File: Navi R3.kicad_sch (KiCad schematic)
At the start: 66 parts, among them J1 USB_C_Receptacle_USB2.0_16P, J2 Conn_01x02_Pin, J3 Conn_01x02_Pin, J4 Conn_01x03_Socket, J5 Conn_02x03_Counter_Clockwise, SW1 SW_Push, SW2 D2FC-F-7N20M, SW3 D2FC-F-7N20M, SW4 D2FC-F-7N20M, SW5 SW_Push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

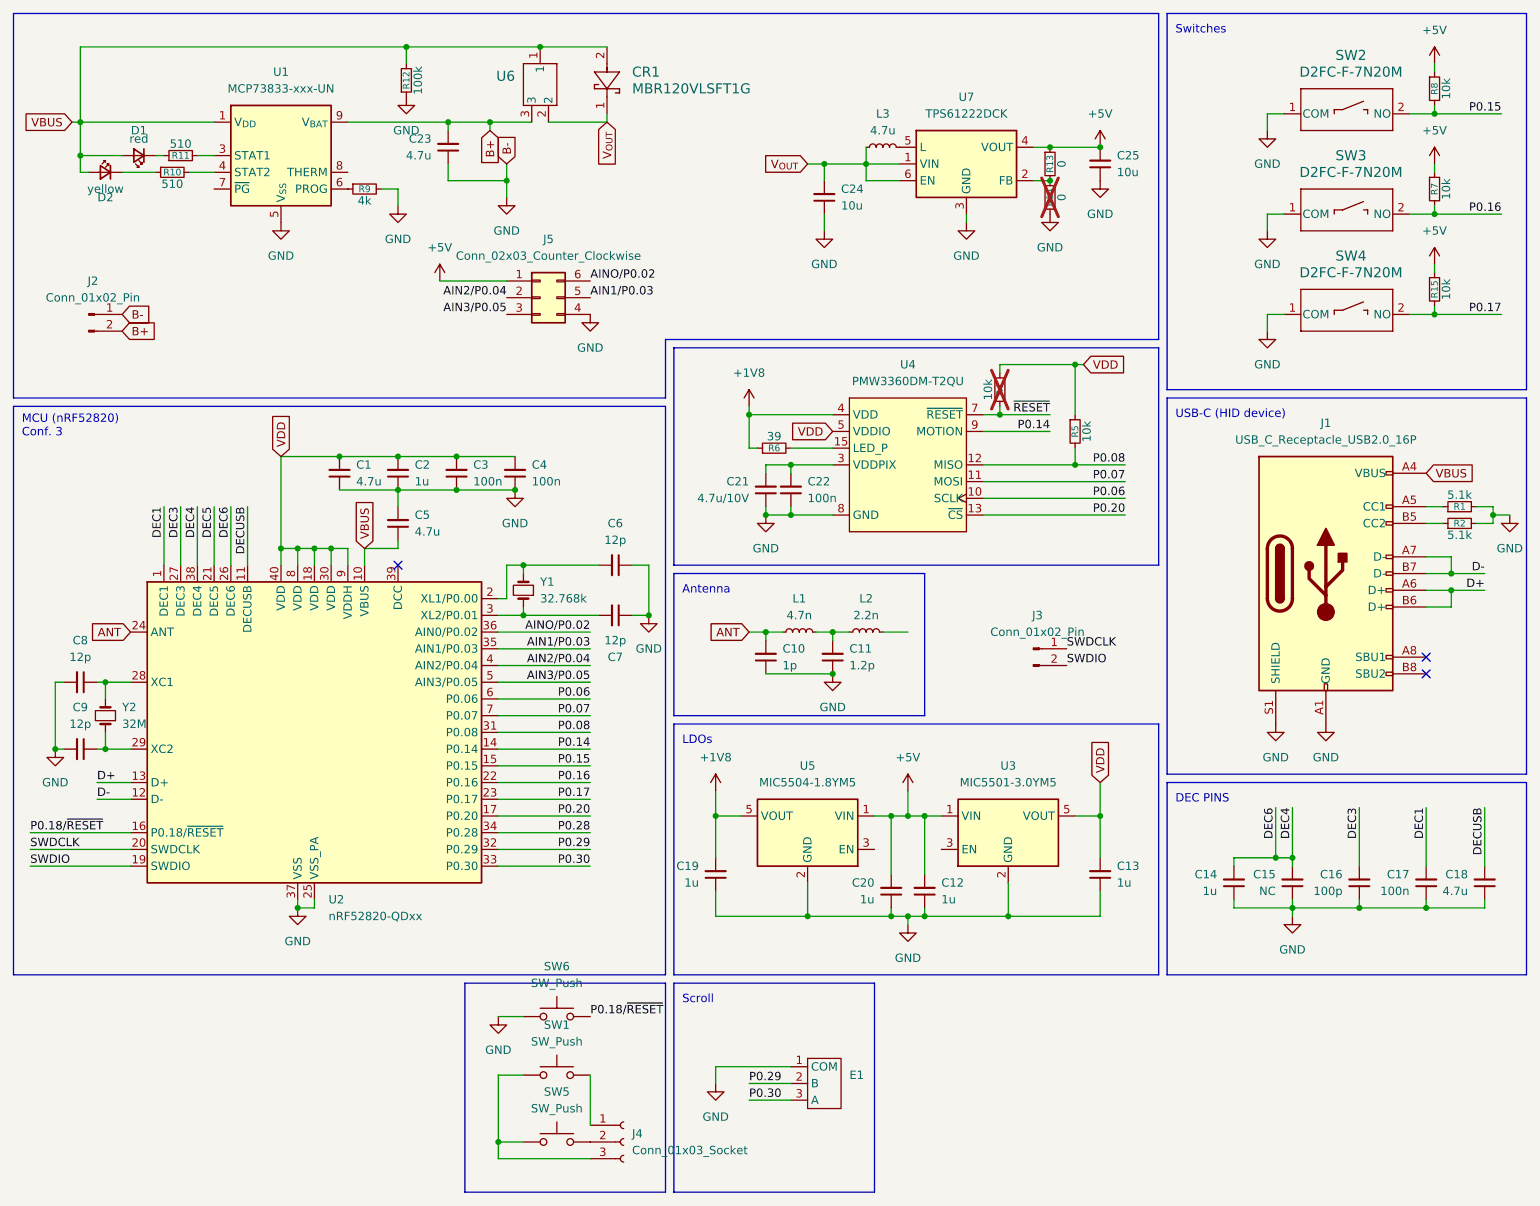
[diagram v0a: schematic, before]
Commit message: Update SWD headers
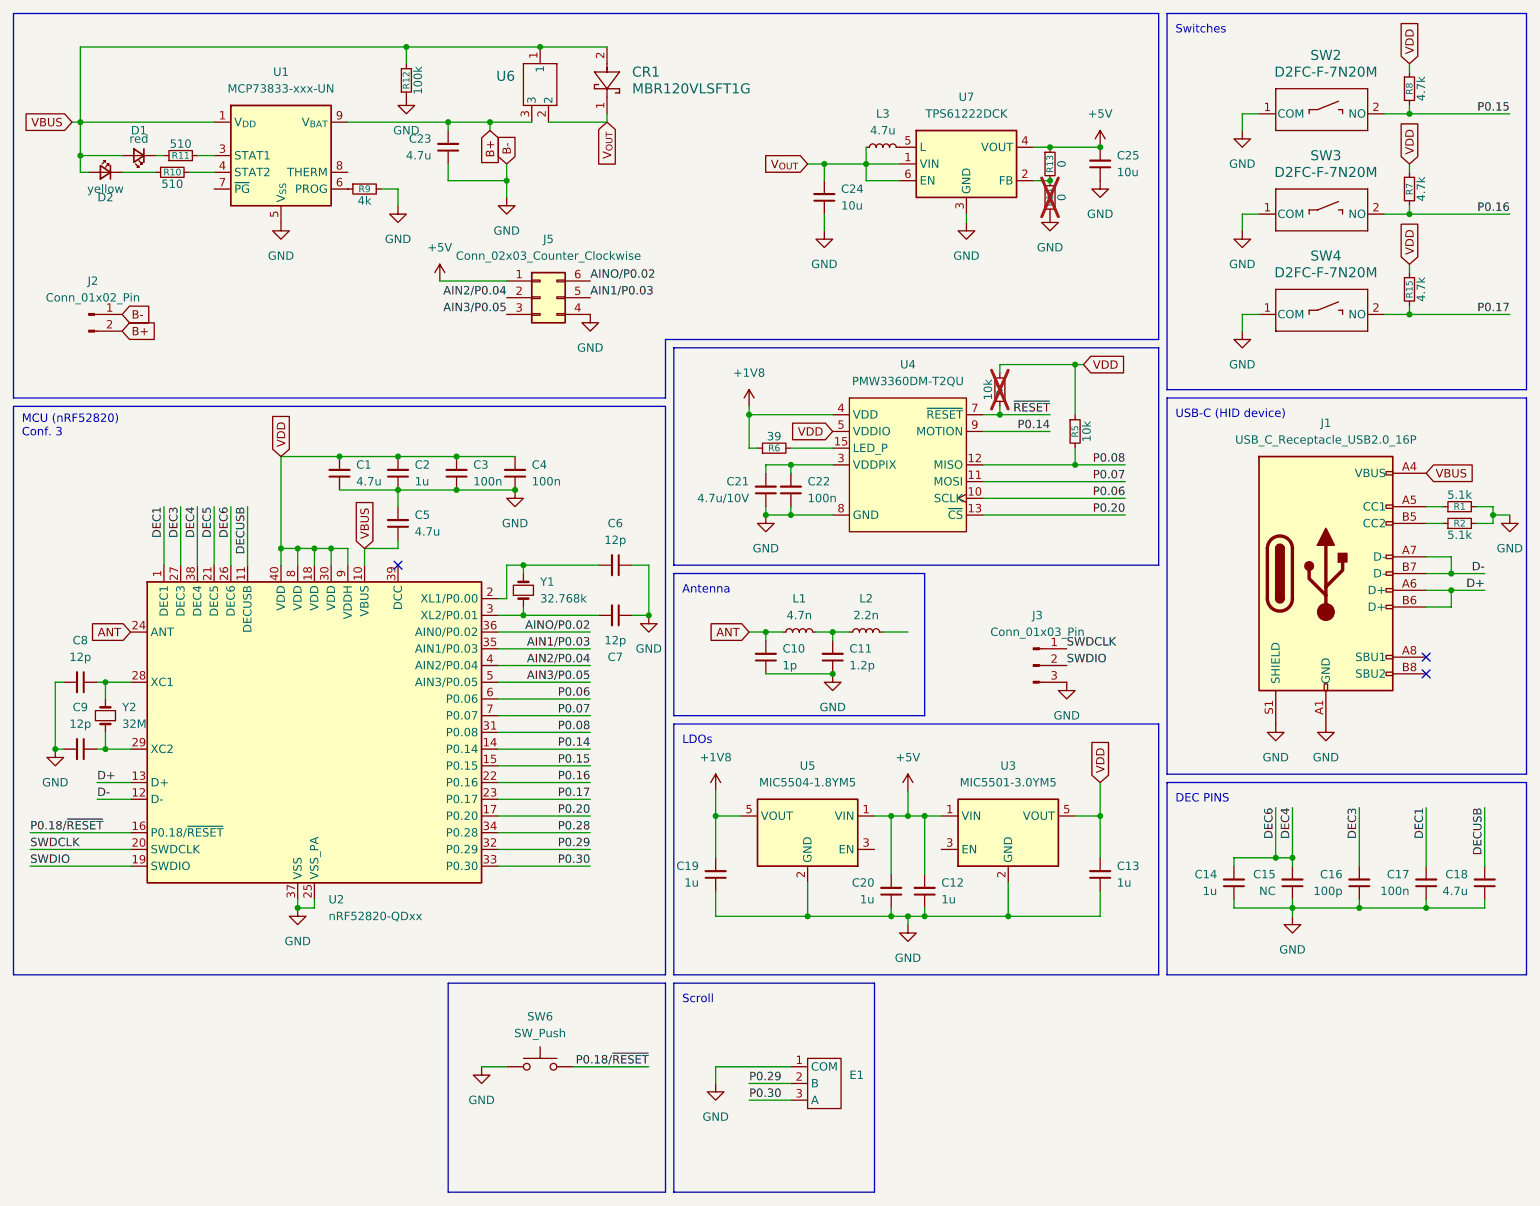
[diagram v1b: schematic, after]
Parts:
- removed J3: Conn_01x02_Pin, Connector_PinHeader_1.00mm:PinHeader_1x02_P1.00mm_Vertical, symbol Connector:Conn_01x02_Pin
- removed J4: Conn_01x03_Socket, Connector_PinSocket_1.00mm:PinSocket_1x03_P1.00mm_Vertical, symbol Connector:Conn_01x03_Socket
- removed SW1, SW5: SW_Push, Button_Switch_THT:SW_PUSH_6mm_H4.3mm, symbol Switch:SW_Push
- added J3: Conn_01x03_Pin, Connector_PinHeader_2.00mm:PinHeader_1x03_P2.00mm_Vertical, symbol Connector:Conn_01x03_Pin
- R15, R7, R8: value 10k -> 4.7k
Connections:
- net +5V: no longer R15.1, R7.1, R8.1
- net GND: now also J3.3 (Pin_3)
- net SWDCLK: now also J3.1 (Pin_1)
- net SWDIO: now also J3.2 (Pin_2)
- net VDD: now also R15.1, R7.1, R8.1
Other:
- moved on the sheet: R15, R7, R8, SW2, SW3, SW4, SW6
